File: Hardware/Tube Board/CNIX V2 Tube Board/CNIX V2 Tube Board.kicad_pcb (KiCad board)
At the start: 2 copper layers, 185 x 51 mm, 50 parts, among them J1 VDD, J2 GND, J3 Tube Conn, J4 LED, J5 HT, U1 SN75468, U10 IN-4_0, U11 IN-4_1, U12 IN-4_2, U13 IN-4_3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

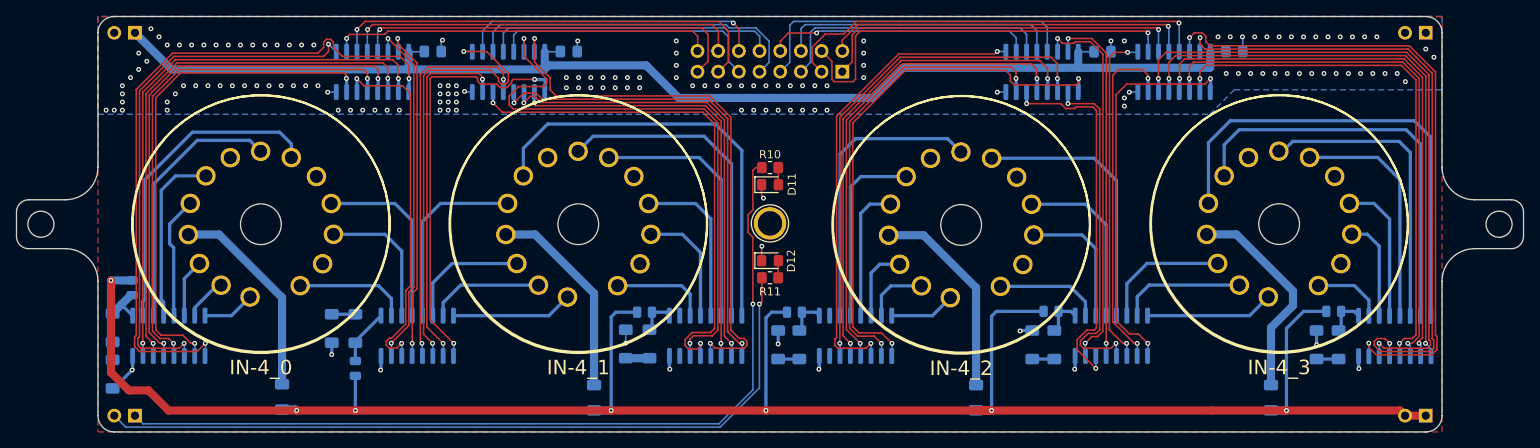
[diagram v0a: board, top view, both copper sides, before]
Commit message: found a bug, that the tubes are wired abckwards, needs to be fixed via new board
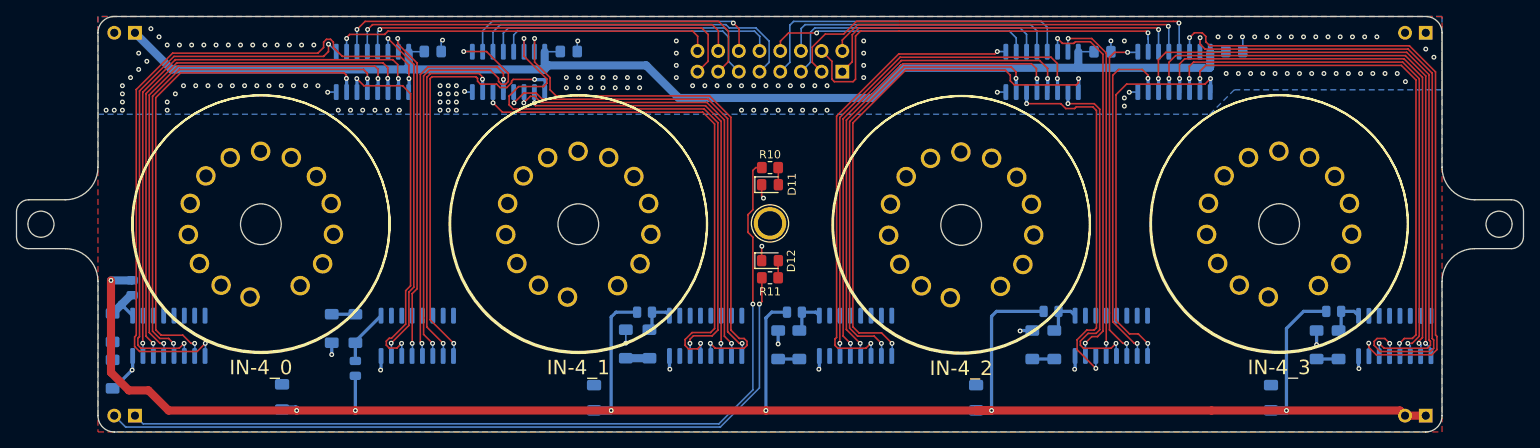
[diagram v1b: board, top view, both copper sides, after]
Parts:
- U10, U11, U12, U13: footprint .Nixie Tubes:IN-4 -> Nixie_Tubes:IN-4
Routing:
- net /T3_K9: track 58.6 -> 0.00 mm
- net /T1_K7: track 53.1 -> 0.00 mm
- net /T3_K7: track 50.5 -> 0.00 mm
- net /T1_K0: track 39.6 -> 0.00 mm
- net /T0_K2: track 39.5 -> 0.00 mm
- net /T3_K0: track 37.2 -> 0.00 mm
- net /T2_K0: track 36.1 -> 0.00 mm
- net /T2_K2: track 33.1 -> 0.00 mm
- net /T0_K0: track 32.1 -> 0.00 mm
- net /T1_K2: track 31.6 -> 0.00 mm
- net /T3_K2: track 28.9 -> 0.00 mm
- net Net-(U13-S): track 26.1 -> 0.00 mm
- net Net-(U12-S): track 25.4 -> 0.00 mm
- net Net-(U10-S): track 25.4 -> 0.00 mm
- net Net-(U11-S): track 25.1 -> 0.00 mm
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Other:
- board text added: "FAIL: Tuibes are wired backwards, needs fixing"

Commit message: added warning for tube fail
https://www.mouser.de/ProductDetail/TDK/C5750X7T2E225K250KA?qs=vG%252BtRDh6KwCR7tEmlFz%2FKw%3D%3D
exit
quit
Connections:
- J1 pad 1: VDD -> GND
- J1 pad 2: GND -> VDD
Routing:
- net VDD: track 153.3 -> 157.5 mm
- net GND: vias 155 -> 154
